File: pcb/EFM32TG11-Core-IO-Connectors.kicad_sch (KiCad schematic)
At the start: 7 parts, among them J2 EXT_PWR, J3 EXT_UART, J4 EXT_I2C, J7 GPIO_LO, J8 GPIO_HI

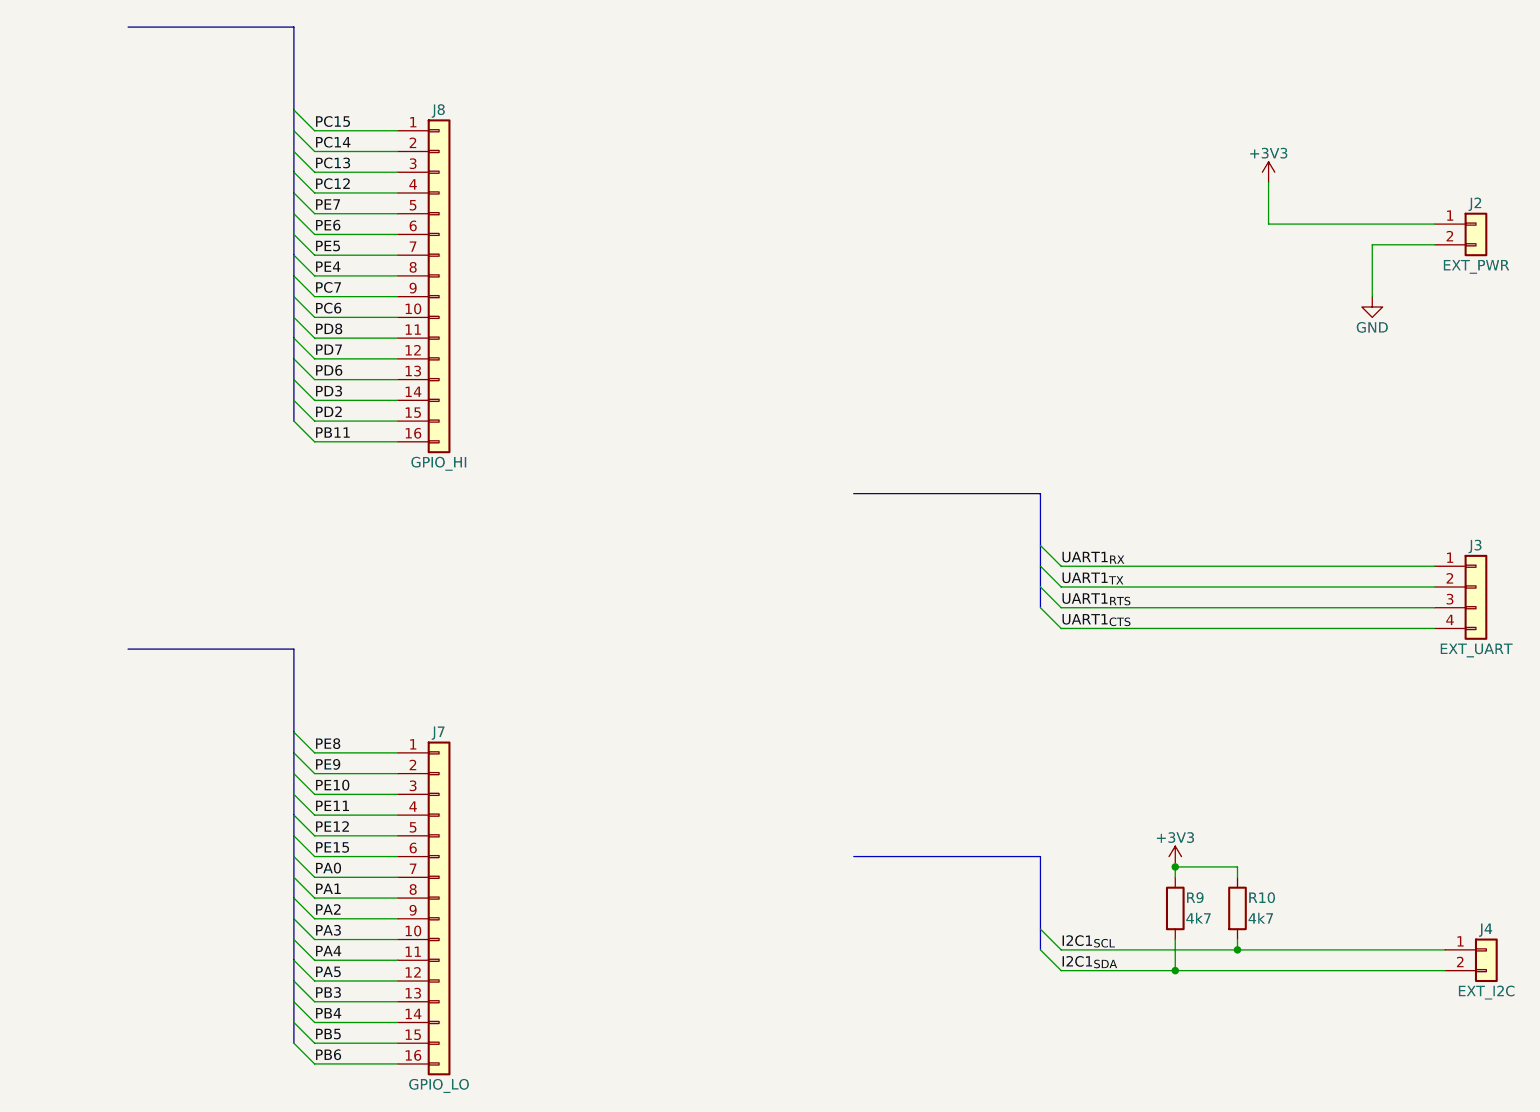
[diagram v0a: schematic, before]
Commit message: Fix Nets for Hierarchical Sheets
Defined busses to pass nets to and from MCU sheet and IO connector
sheet.
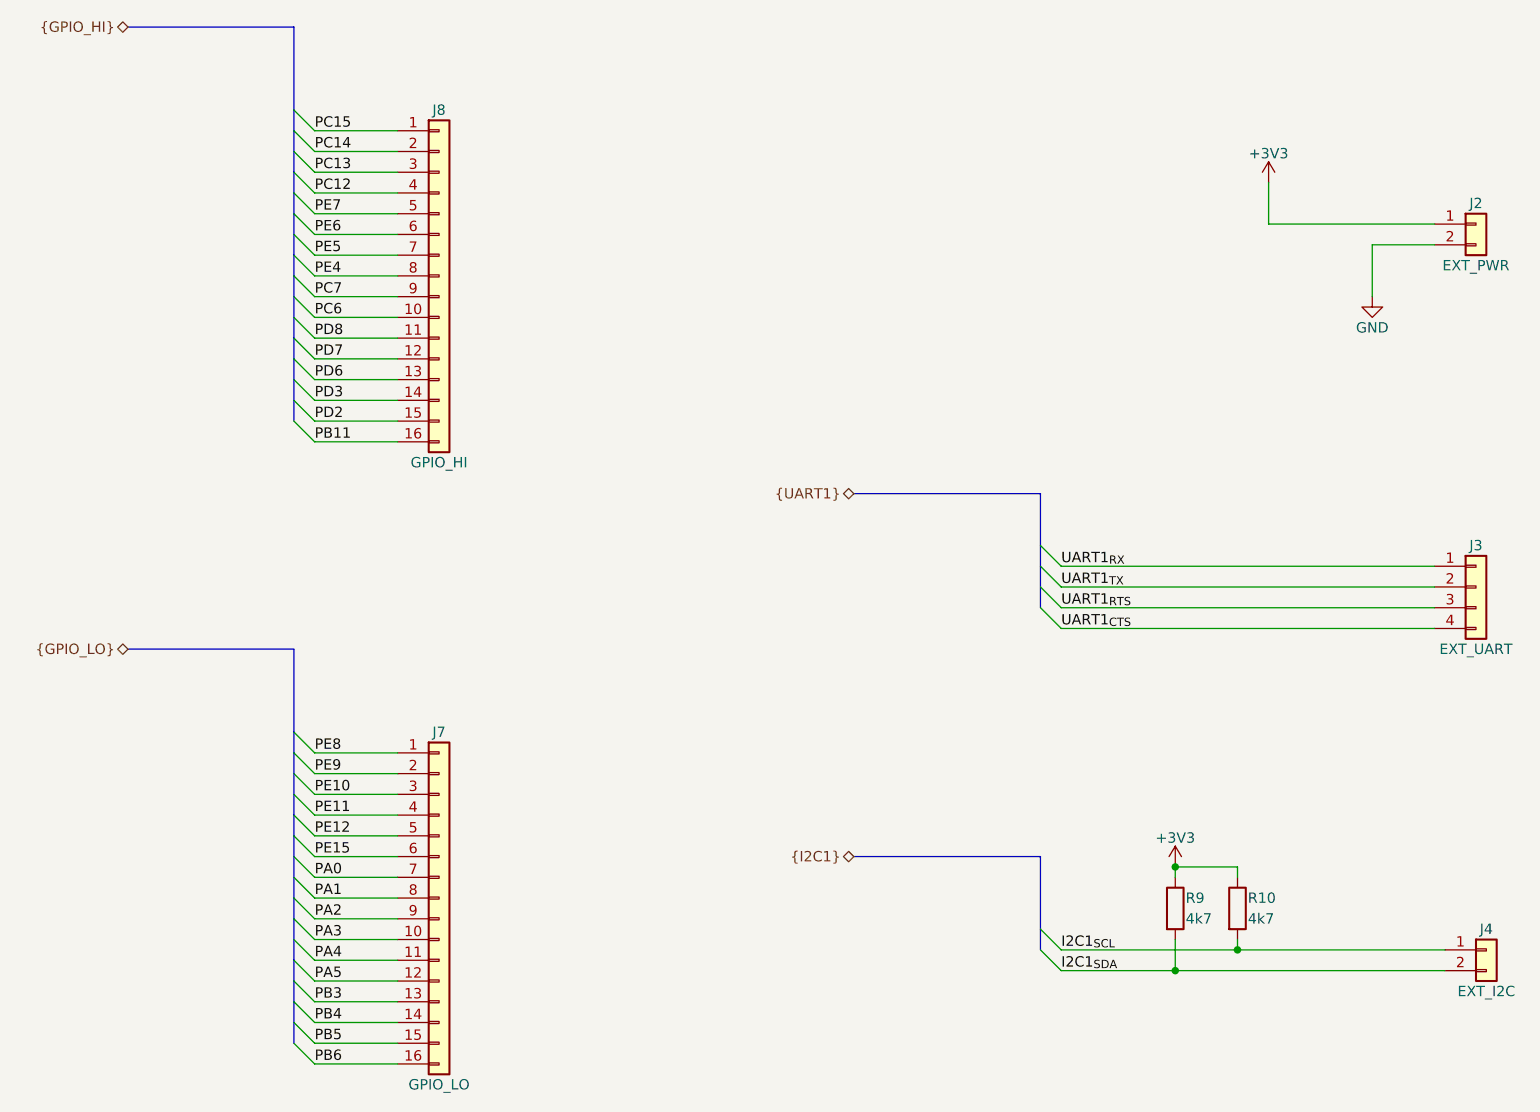
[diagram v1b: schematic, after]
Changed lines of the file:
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@@
     (comment 1 "Rev A: Initial Release")
   )
+  (bus_alias "GPIO_HI" (members "PB11" "PD[2..3]" "PD[6..8]" "PC[6..7]" "PE[4..7]" "PC[12..15]"))
+  (bus_alias "GPIO_LO" (members "PE[8..12]" "PE15" "PA[0..5]" "PB[3..6]"))
   (junction (at 179.07 140.97) (diameter 0) (color 0 0 0 0)
   )
@@
     (effects (font (size 1.27 1.27)) (justify left bottom))
   )
+  (hierarchical_label "{GPIO_LO}" (shape bidirectional) (at 50.8 101.6 180)
+    (effects (font (size 1.27 1.27)) (justify right))
+  )
+  (hierarchical_label "{I2C1}" (shape bidirectional) (at 139.7 127 180)
+    (effects (font (size 1.27 1.27)) (justify right))
+  )
+  (hierarchical_label "{GPIO_HI}" (shape bidirectional) (at 50.8 25.4 180)
+    (effects (font (size 1.27 1.27)) (justify right))
+  )
+  (hierarchical_label "{UART1}" (shape bidirectional) (at 139.7 82.55 180)
+    (effects (font (size 1.27 1.27)) (justify right))
+  )
   (symbol (lib_id "power:+3V3") (at 190.5 44.45 0) (unit 1)
